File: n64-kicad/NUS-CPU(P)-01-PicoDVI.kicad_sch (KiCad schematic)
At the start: 3 parts, among them U5 Pico

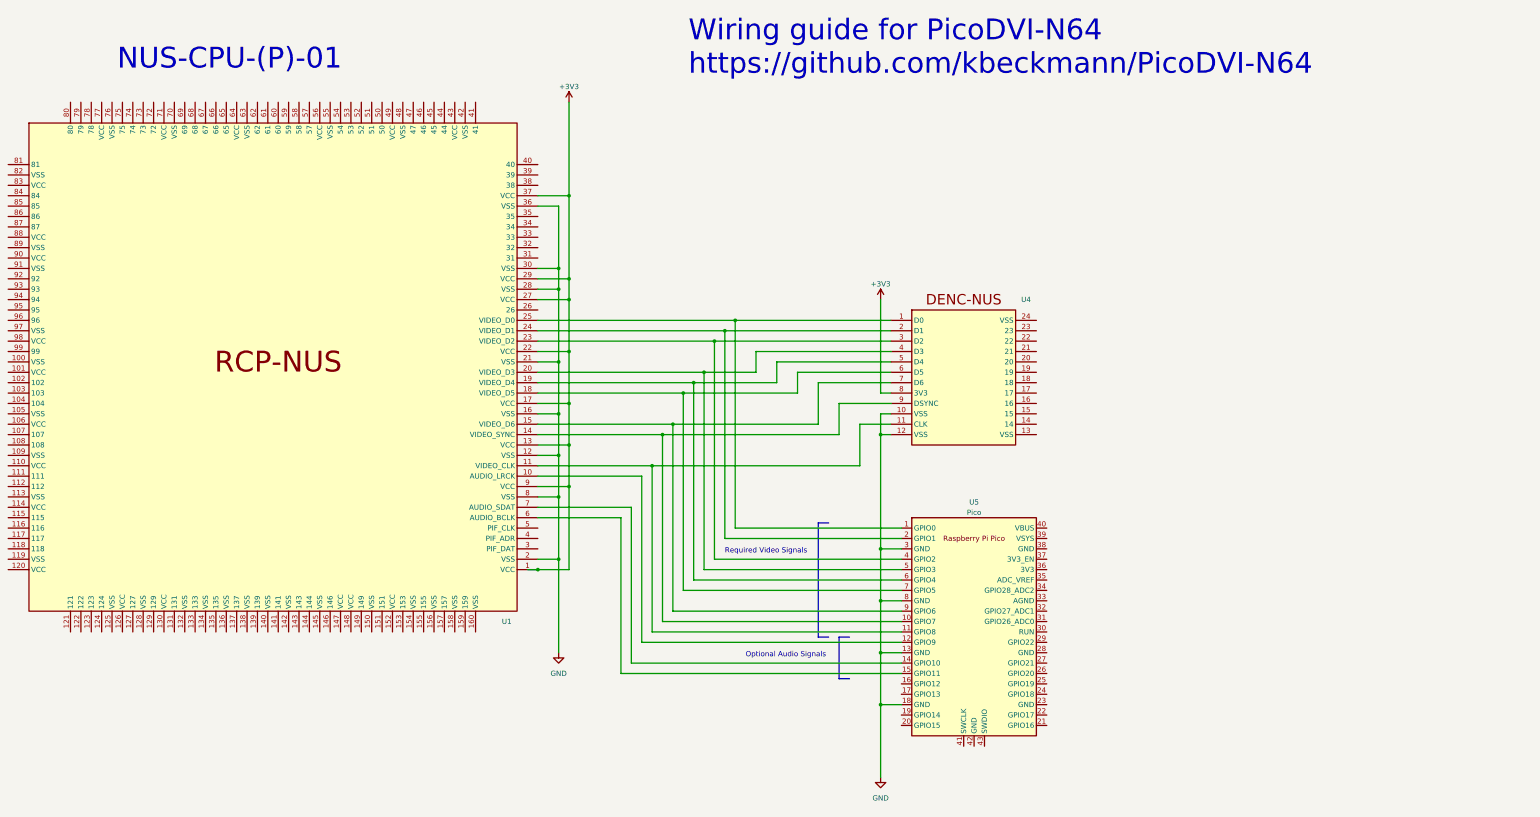
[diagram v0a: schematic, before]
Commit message: Fix labels and update PDF
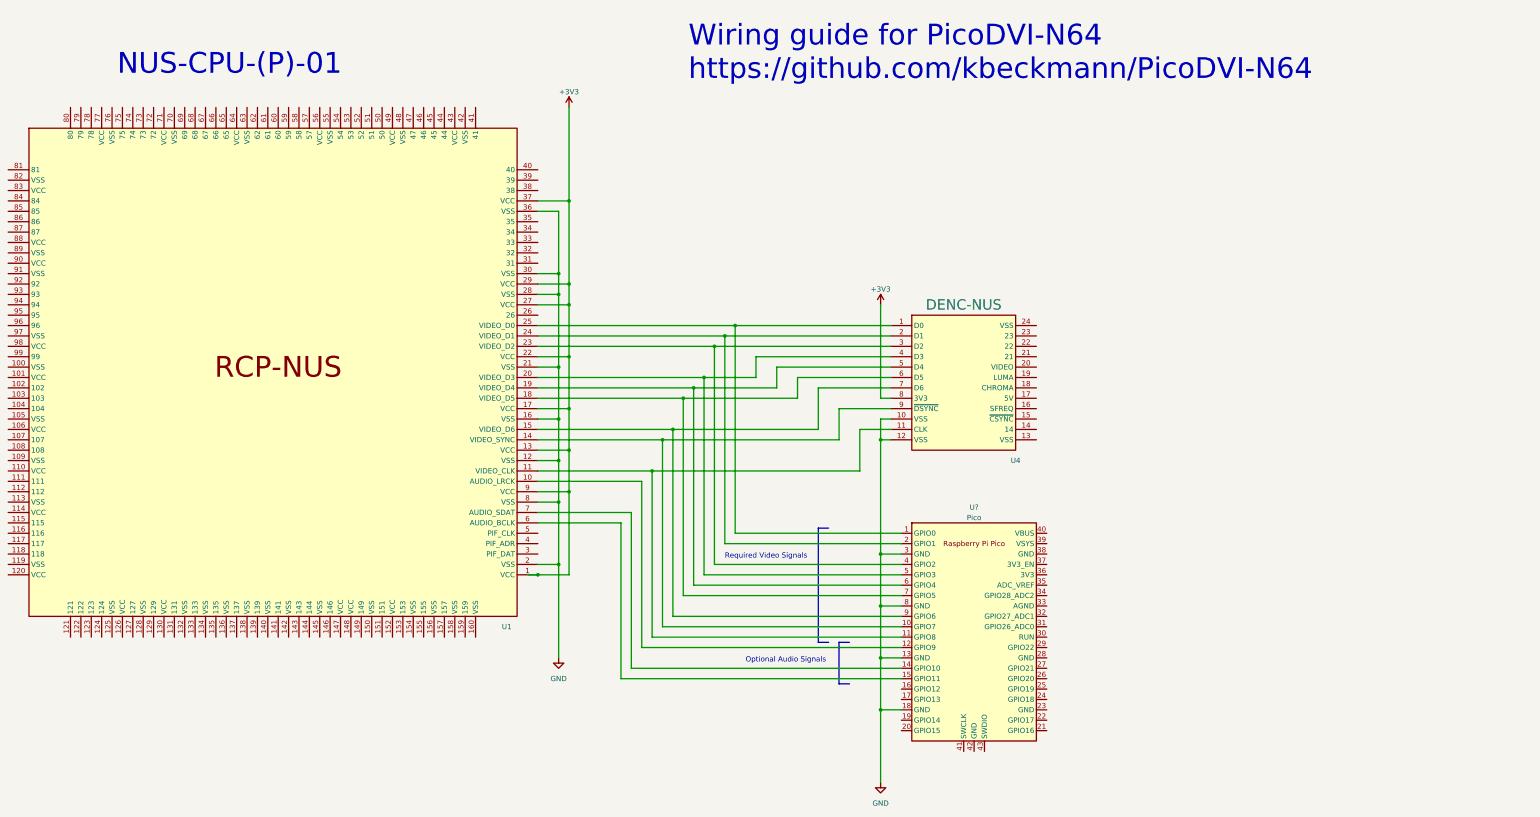
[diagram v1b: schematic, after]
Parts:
- U4: value ~ -> DENC-NUS
- renumbered U5 to U?
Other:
- moved on the sheet: U1, U?
